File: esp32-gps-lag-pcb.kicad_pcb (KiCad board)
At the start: 2 copper layers, 60 x 85 mm, 9 parts, among them J1 GPS UART, J2 eInk display, SW1 SW_Push, U1 ESP32-DevKitC

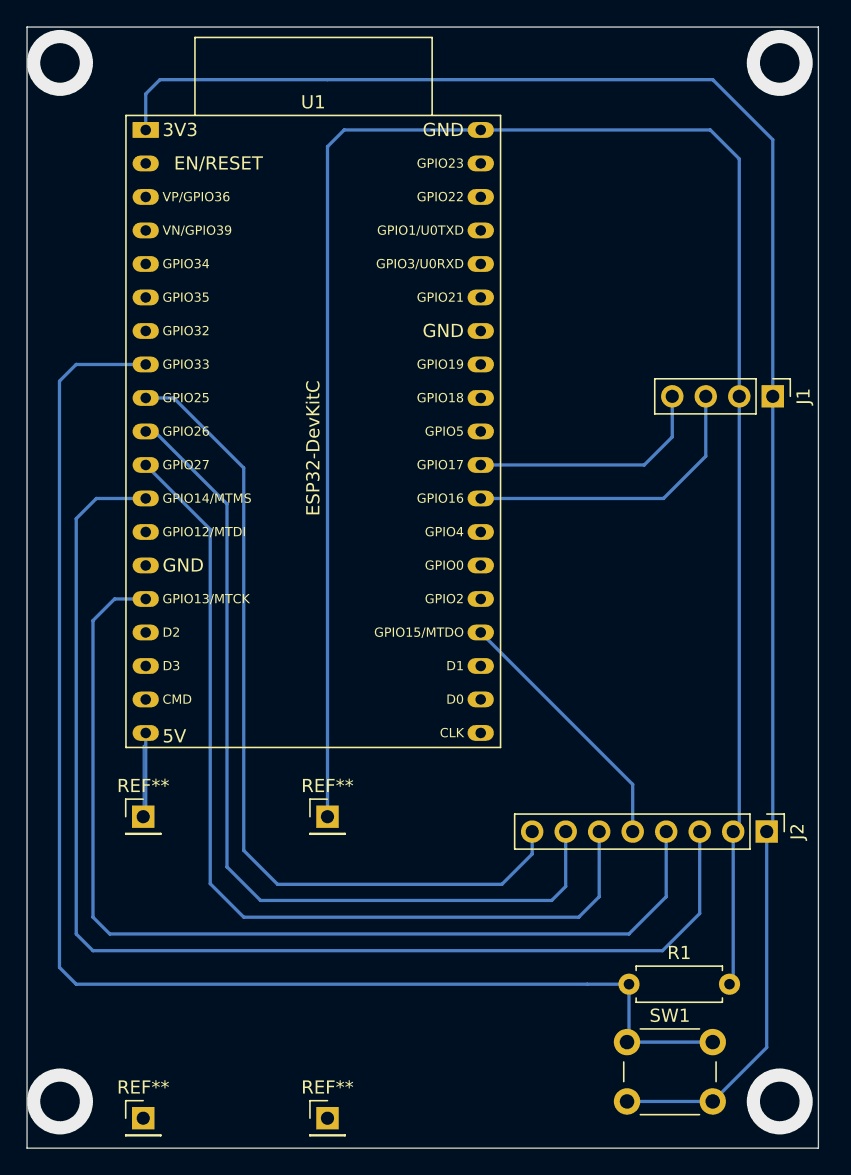
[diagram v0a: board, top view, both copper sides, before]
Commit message: Battery capacity measurement, new GNSS module, etc.
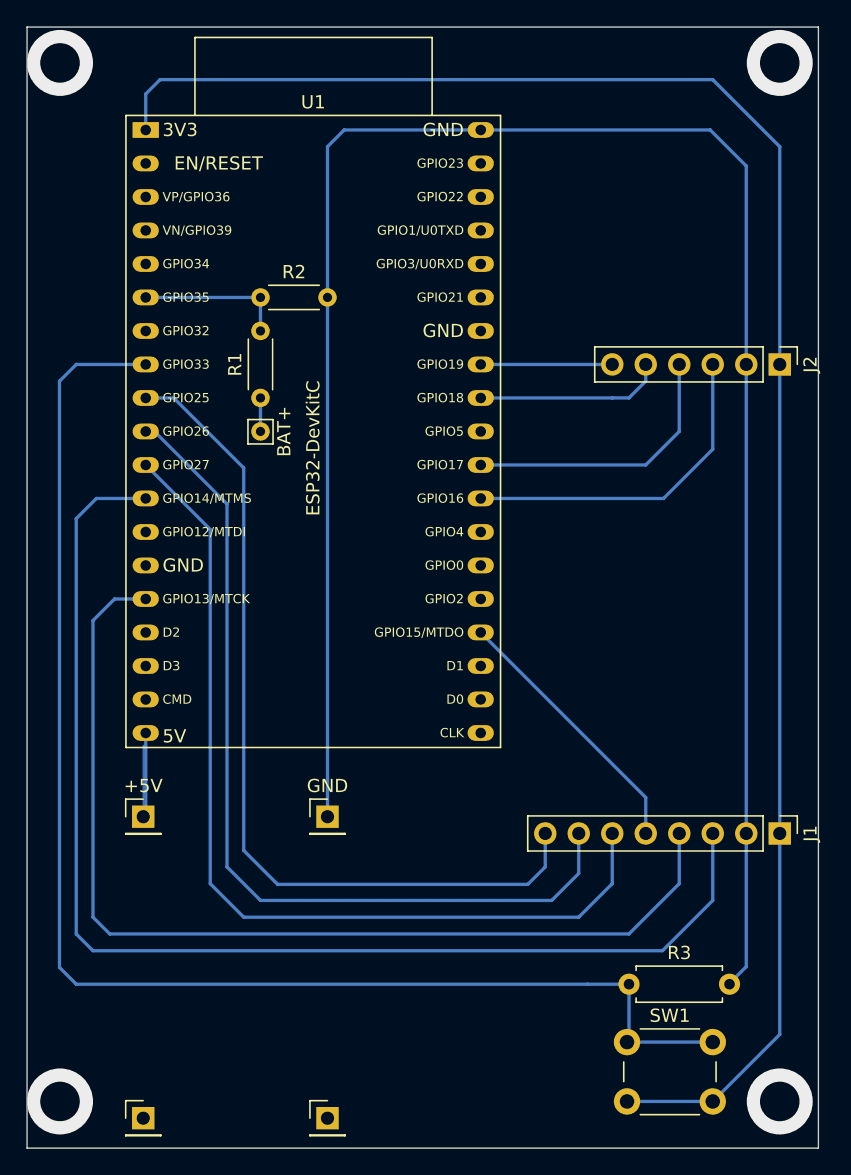
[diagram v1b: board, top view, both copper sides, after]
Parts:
- added BAT+: Pin_D0.7mm_L6.5mm_W1.8mm_FlatFork, Connector_Pin:Pin_D0.7mm_L6.5mm_W1.8mm_FlatFork, F.Cu at (139.7, 73.7)
- added R2: 100K, Resistor_THT:R_Axial_DIN0204_L3.6mm_D1.6mm_P5.08mm_Horizontal, F.Cu at (139.7, 63.5)
- added R3: 10k, Resistor_THT:R_Axial_DIN0207_L6.3mm_D2.5mm_P7.62mm_Horizontal, F.Cu at (167.6, 115.6)
- J1: value GPS UART -> eInk display; footprint Connector_PinHeader_2.54mm:PinHeader_1x04_P2.54mm_Vertical -> Connector_PinHeader_2.54mm:PinHeader_1x08_P2.54mm_Vertical
- J2: value eInk display -> GNSS; footprint Connector_PinHeader_2.54mm:PinHeader_1x08_P2.54mm_Vertical -> Connector_PinHeader_2.54mm:PinHeader_1x06_P2.54mm_Vertical
- R1: value R10k -> 100K; footprint Resistor_THT:R_Axial_DIN0207_L6.3mm_D2.5mm_P7.62mm_Horizontal -> Resistor_THT:R_Axial_DIN0204_L3.6mm_D1.6mm_P5.08mm_Horizontal
- moved R1 52.5 mm to (139.7, 71.1), turned to 90 degrees
- moved J2 35.4 mm to (179.1, 68.6)
- moved J1 33.1 mm to (179.1, 104.1)
- renumbered REF** to +5V, REF** to GND
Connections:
- R1 pad 1: Net-(U1-32K_XN/GPIO33/ADC1_CH5) -> +4V
- R1 pad 2: GND -> Net-(U1-VDET_2/GPIO35/ADC1_CH7)
- U1 pad 10: Net-(J2-Pin_7) -> Net-(J1-Pin_7)
- U1 pad 11: Net-(J2-Pin_6) -> Net-(J1-Pin_6)
- U1 pad 12: Net-(J2-Pin_3) -> Net-(J1-Pin_3)
- U1 pad 15: Net-(J2-Pin_4) -> Net-(J1-Pin_4)
- U1 pad 23: Net-(J2-Pin_5) -> Net-(J1-Pin_5)
- U1 pad 27: Net-(J1-Pin_3) -> Net-(J2-Pin_3)
- U1 pad 28: Net-(J1-Pin_4) -> Net-(J2-Pin_4)
- U1 pad 30: unconnected-(U1-GPIO18-Pad30) -> Net-(J2-Pin_5)
- U1 pad 31: unconnected-(U1-GPIO19-Pad31) -> Net-(J2-Pin_6)
- U1 pad 6: unconnected-(U1-VDET_2/GPIO35/ADC1_CH7-Pad6) -> Net-(U1-VDET_2/GPIO35/ADC1_CH7)
- U1 pad 9: Net-(J2-Pin_8) -> Net-(J1-Pin_8)
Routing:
- net Net-(J1-Pin_6): track 0.00 -> 70.2 mm
- net Net-(J1-Pin_3): track 22.9 -> 92.0 mm
- net Net-(J1-Pin_7): track 0.00 -> 67.6 mm
- net Net-(J2-Pin_7): track 67.3 -> 0.00 mm
- net Net-(J2-Pin_3): track 92.6 -> 25.6 mm
- net Net-(J1-Pin_8): track 0.00 -> 65.6 mm
- net Net-(J2-Pin_8): track 64.2 -> 0.00 mm
- net Net-(J2-Pin_6): track 69.9 -> 9.97 mm
- net Net-(J1-Pin_4): track 18.5 -> 76.7 mm
- net Net-(J2-Pin_4): track 77.3 -> 21.2 mm
- net Net-(J1-Pin_5): track 0.00 -> 20.4 mm
- net Net-(U1-VDET_2/GPIO35/ADC1_CH7): track 0.00 -> 11.2 mm
- net Net-(J2-Pin_5): track 19.9 -> 14.3 mm
- net +4V: track 0.00 -> 2.54 mm
- net GND: track 147.0 -> 145.9 mm
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
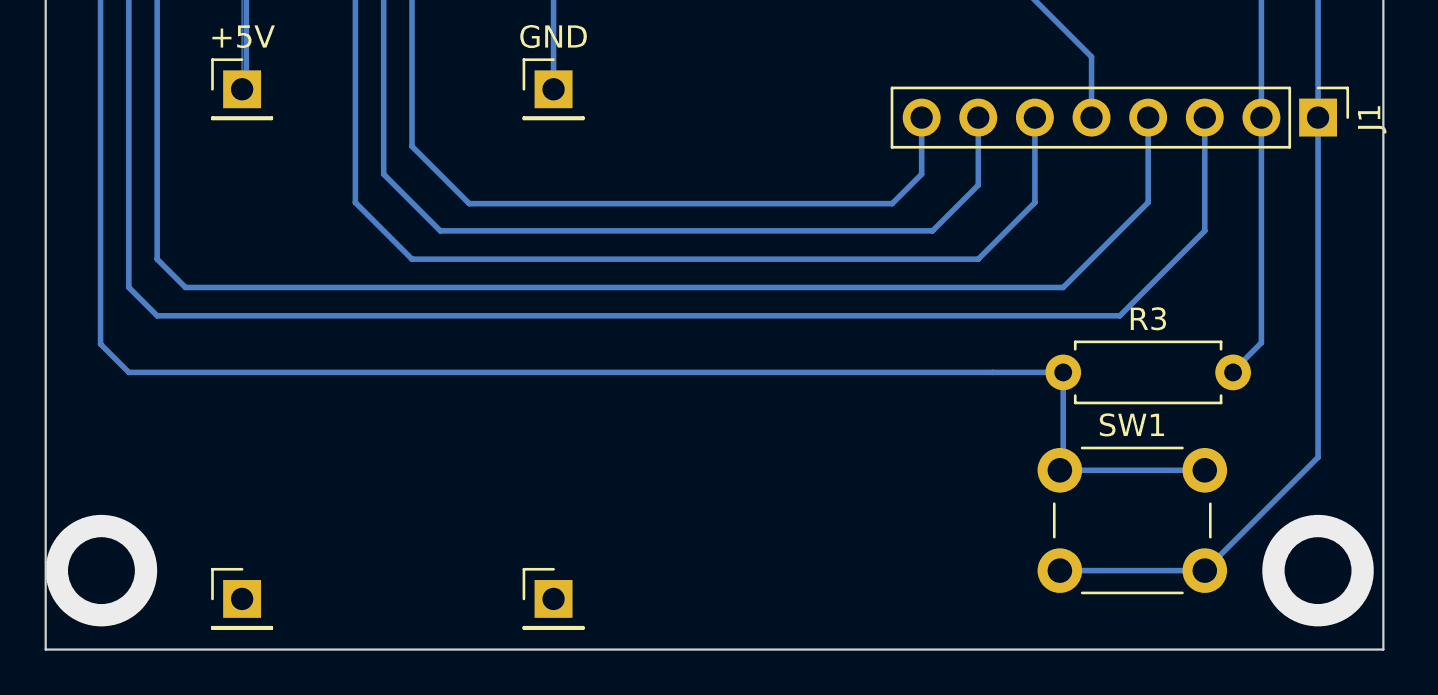
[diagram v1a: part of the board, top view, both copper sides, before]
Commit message: Change button and resistor footprints.
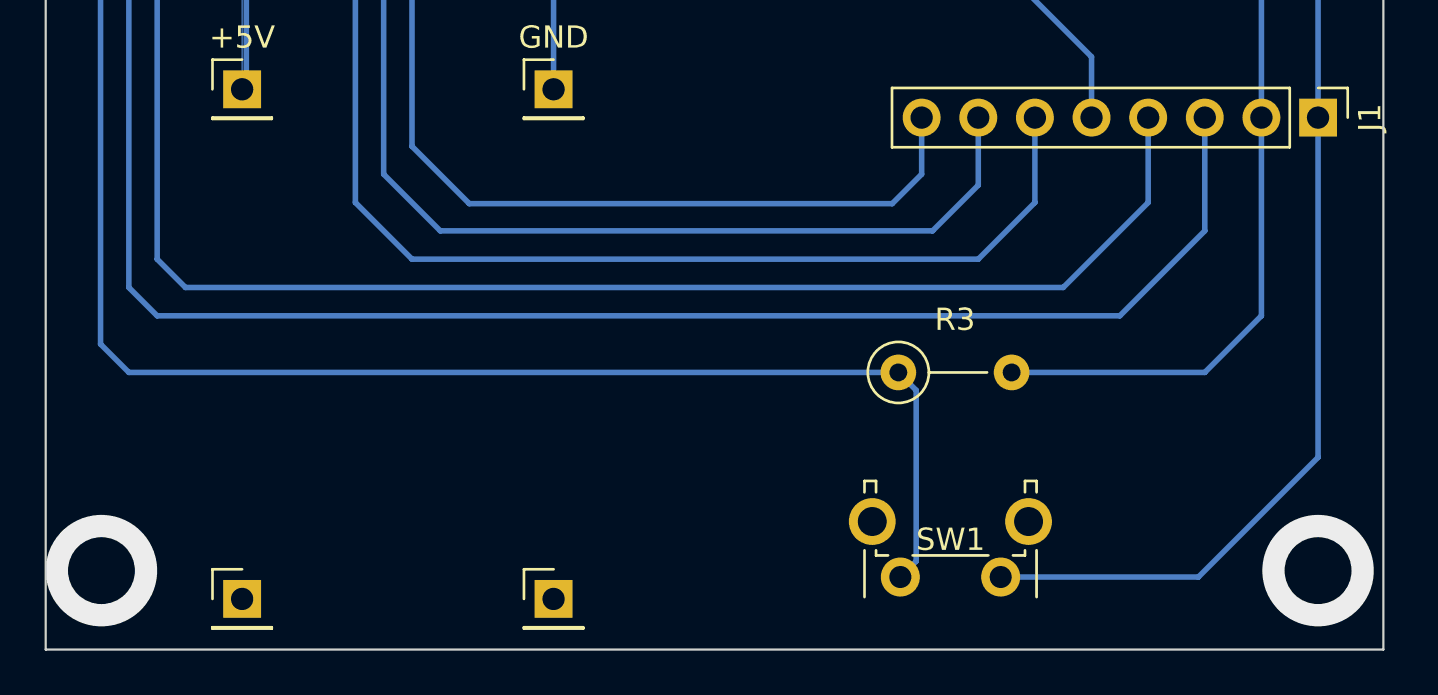
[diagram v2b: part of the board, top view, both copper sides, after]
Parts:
- R3: footprint Resistor_THT:R_Axial_DIN0207_L6.3mm_D2.5mm_P7.62mm_Horizontal -> Resistor_THT:R_Axial_DIN0207_L6.3mm_D2.5mm_P5.08mm_Vertical
- SW1: footprint Button_Switch_THT:SW_PUSH_6mm_H4.3mm -> Button_Switch_THT:SW_Tactile_SPST_Angled_PTS645Vx39-2LFS
- moved R3 7.39 mm to (160.2, 115.6)
- moved SW1 5.47 mm to (164.8, 124.7), turned to 180 degrees
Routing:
- net GND: track 145.9 -> 155.1 mm
- net Net-(U1-32K_XN/GPIO33/ADC1_CH5): track 106.2 -> 97.6 mm
- net +3.3V: track 133.5 -> 136.3 mm
